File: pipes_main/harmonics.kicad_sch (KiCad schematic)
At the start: 70 parts, among them U10 CD4046, U11 CD4046, U12 CD4046, U13 CD4017, U14 CD4017, U15 CD4017, U16 CD4046, U17 CD4046, U18 CD4017, U19 CD4017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

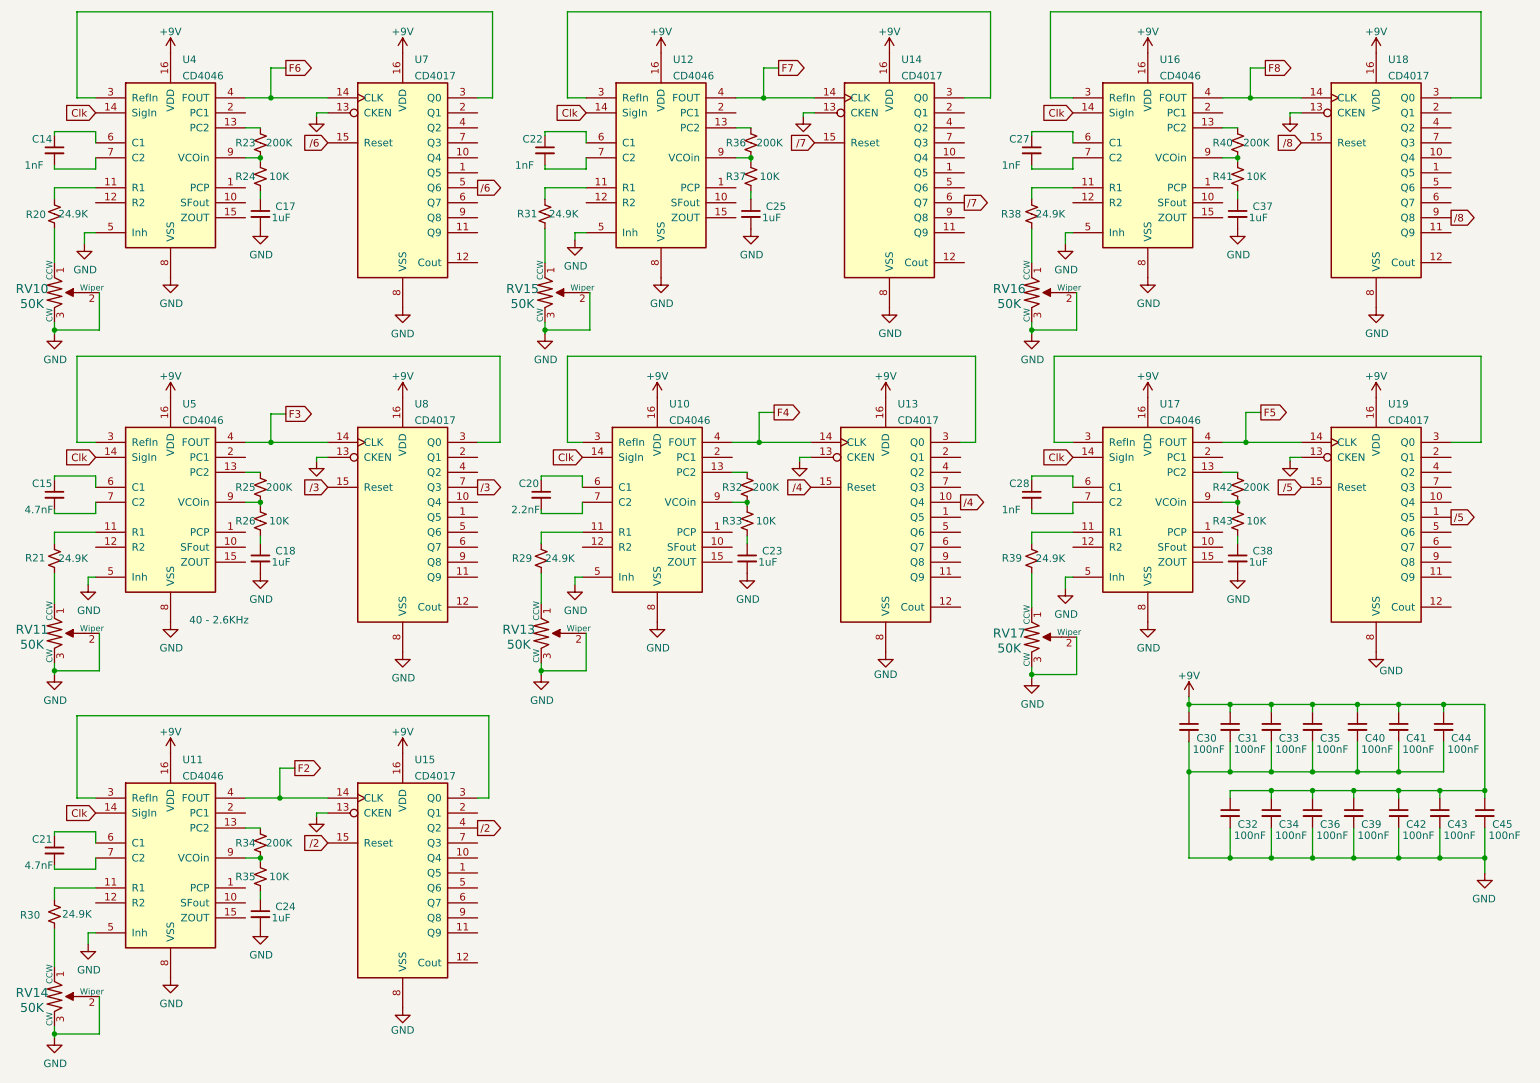
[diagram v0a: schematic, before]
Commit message: Adds digikey bom merge. Uses local graphics for panel.
Adds bambooh graphics
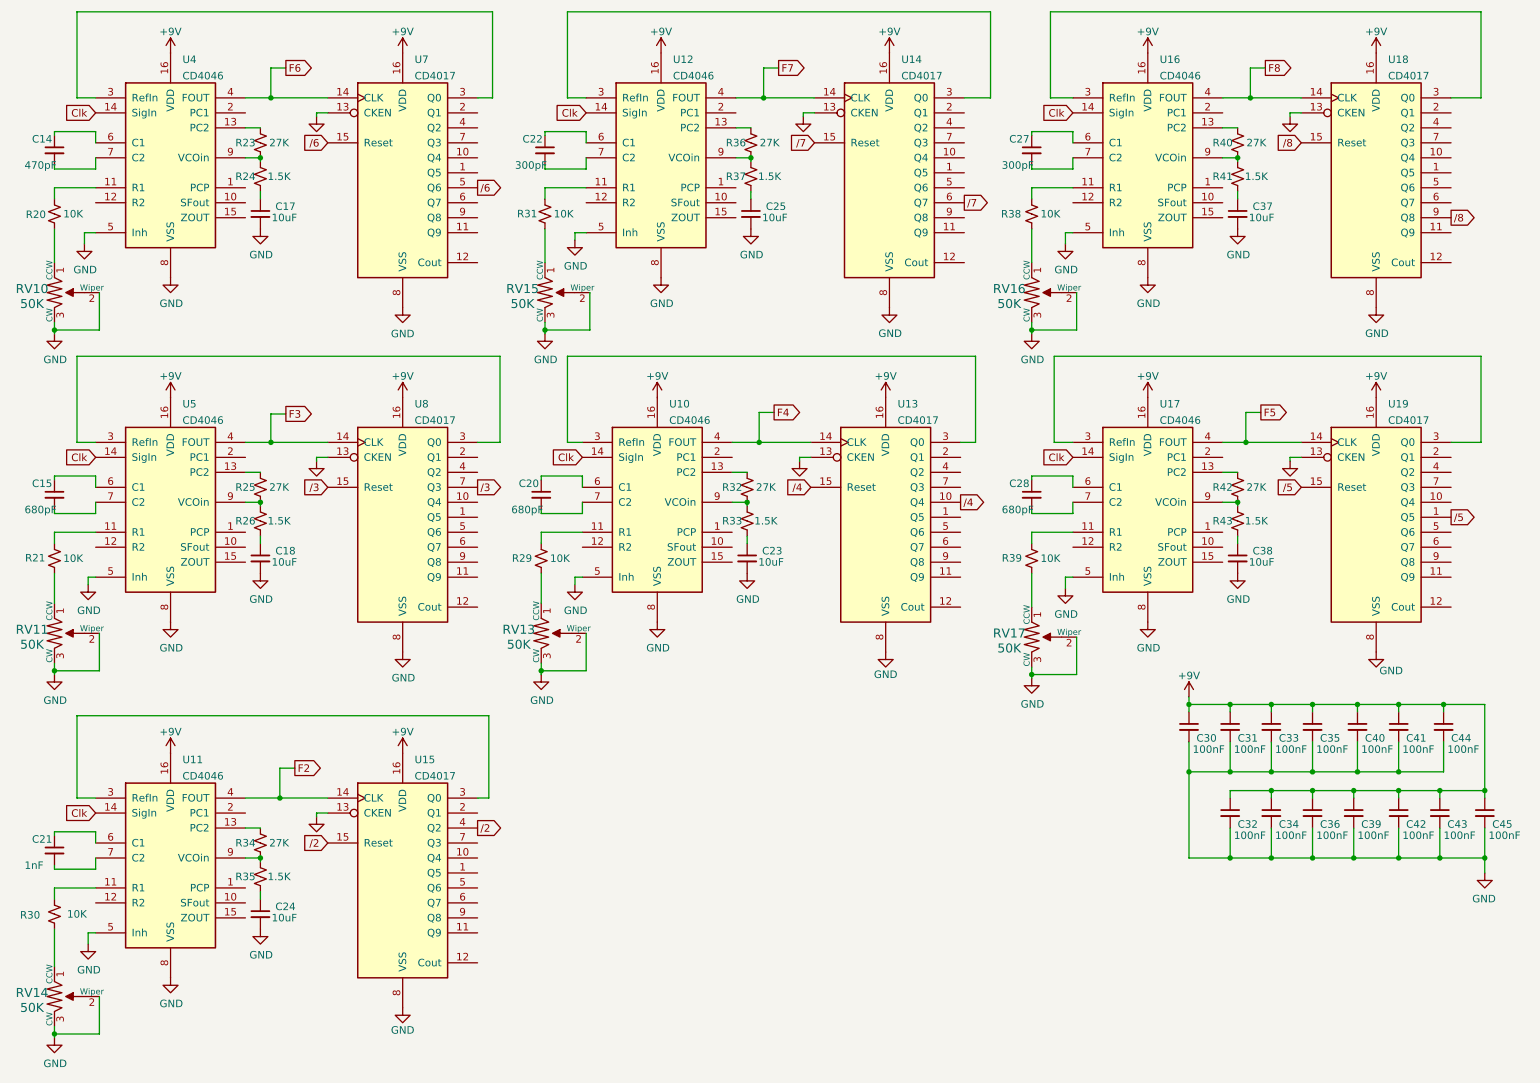
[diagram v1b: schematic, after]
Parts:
- C14: value 1nF -> 470pF; LCSC Part # C46653 -> C1743
- C15: value 4.7nF -> 680pF; LCSC Part # C107104 -> C520092
- C17, C18, C23, C24, C25, C37, C38: value 1uF -> 10uF; LCSC Part # C28323 -> C15850
- C20: value 2.2nF -> 680pF; LCSC Part # C28260 -> C520092
- C21: value 4.7nF -> 1nF; LCSC Part # C107104 -> C46653
- C22, C27: value 1nF -> 300pF; LCSC Part # C46653 -> C282698
- C28: value 1nF -> 680pF; LCSC Part # C46653 -> C520092
- R20, R21, R29, R30, R31, R38, R39: value 24.9K -> 10K; LCSC Part # C137761 -> C25804
- R23, R25, R32, R34, R36, R40, R42: value 200K -> 27K; LCSC Part # C17539 -> C17593
- R24, R26, R33, R35, R37, R41, R43: value 10K -> 1.5K; LCSC Part # C17414 -> C4310
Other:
- note removed: "40 - 2.6KHz"
